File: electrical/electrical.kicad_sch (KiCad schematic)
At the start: 0 parts

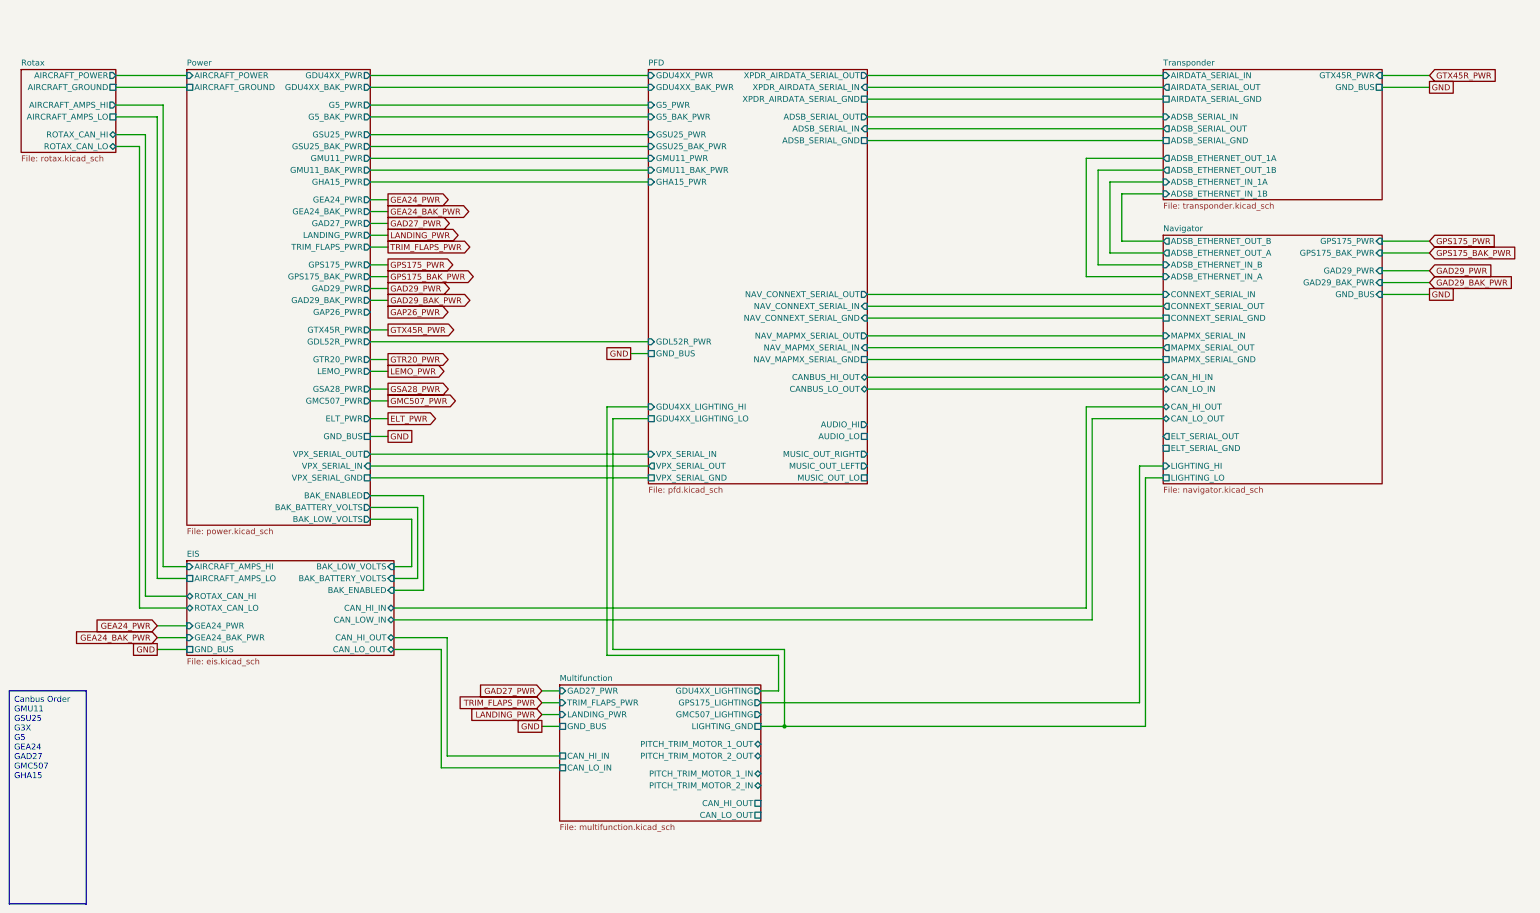
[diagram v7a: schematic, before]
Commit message: Added autopilot
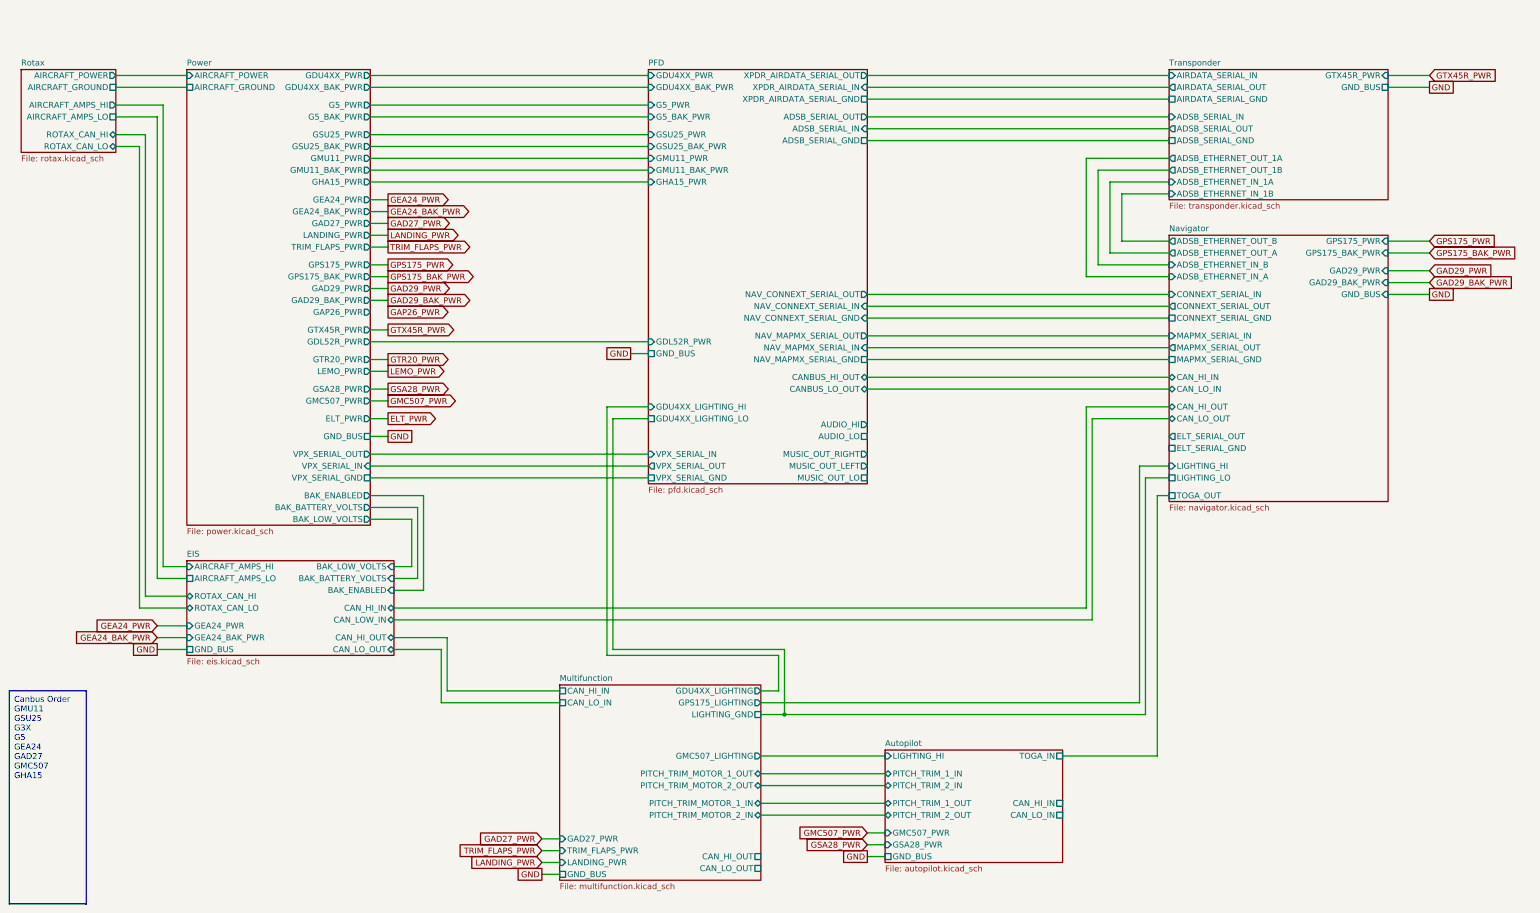
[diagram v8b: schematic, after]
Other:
- added sheet Autopilot (autopilot.kicad_sch)
- sheet Navigator ports: added TOGA_OUT; removed none
